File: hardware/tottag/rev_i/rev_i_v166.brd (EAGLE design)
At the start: 68.1 x 36.9 mm, 185 parts, among them J1 USB4110-GF-A, J2 TC2030-JLINK-NL-2SIDE, J3 TC2030-JLINK-NL-2SIDE, J4 MOLEX-PICO-SPOX-3SIDE, Q1 CSD75207W15, Q2 MOSFET-NCHANNELXFDN-3, U1 APOLLO4_BLUE_SOC_BGA, U2 DW3210, U3 BQ24040, U4 BQ51013B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

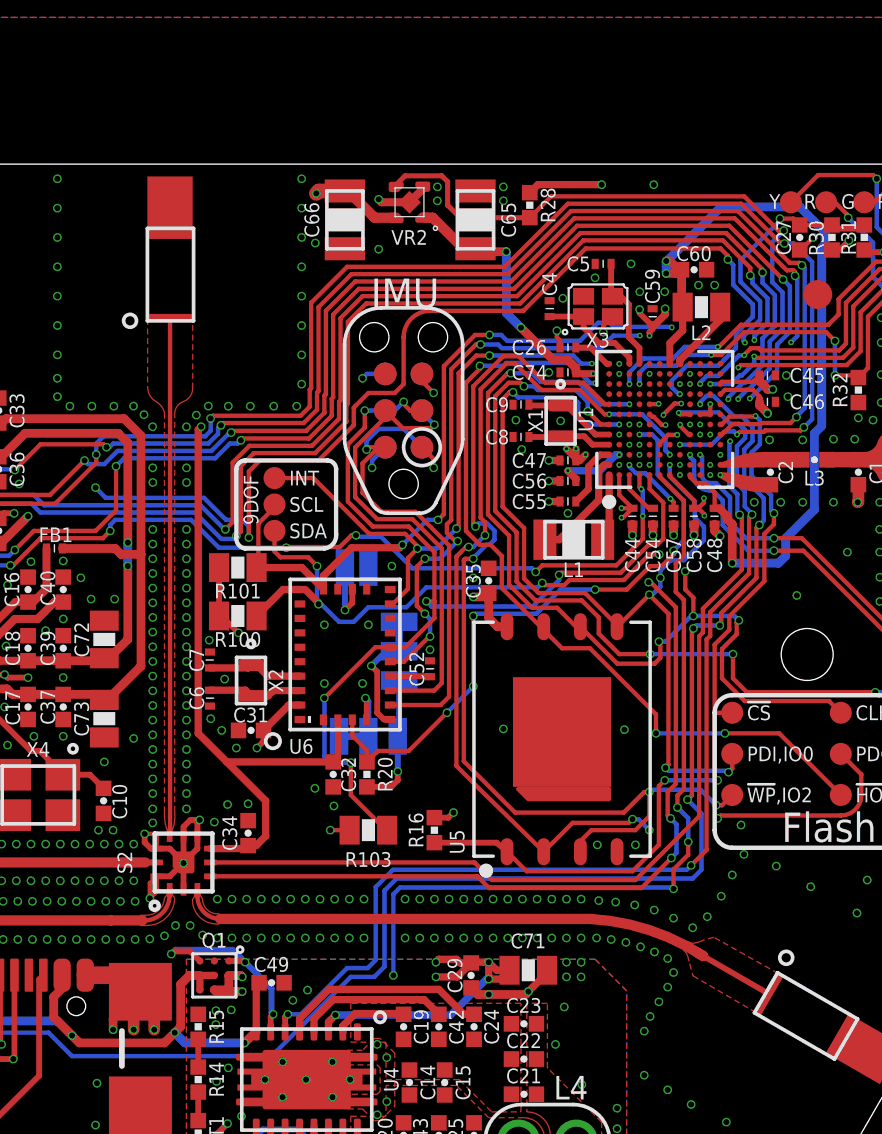
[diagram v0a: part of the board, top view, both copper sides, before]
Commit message: fix VR2 footprint; add BOM
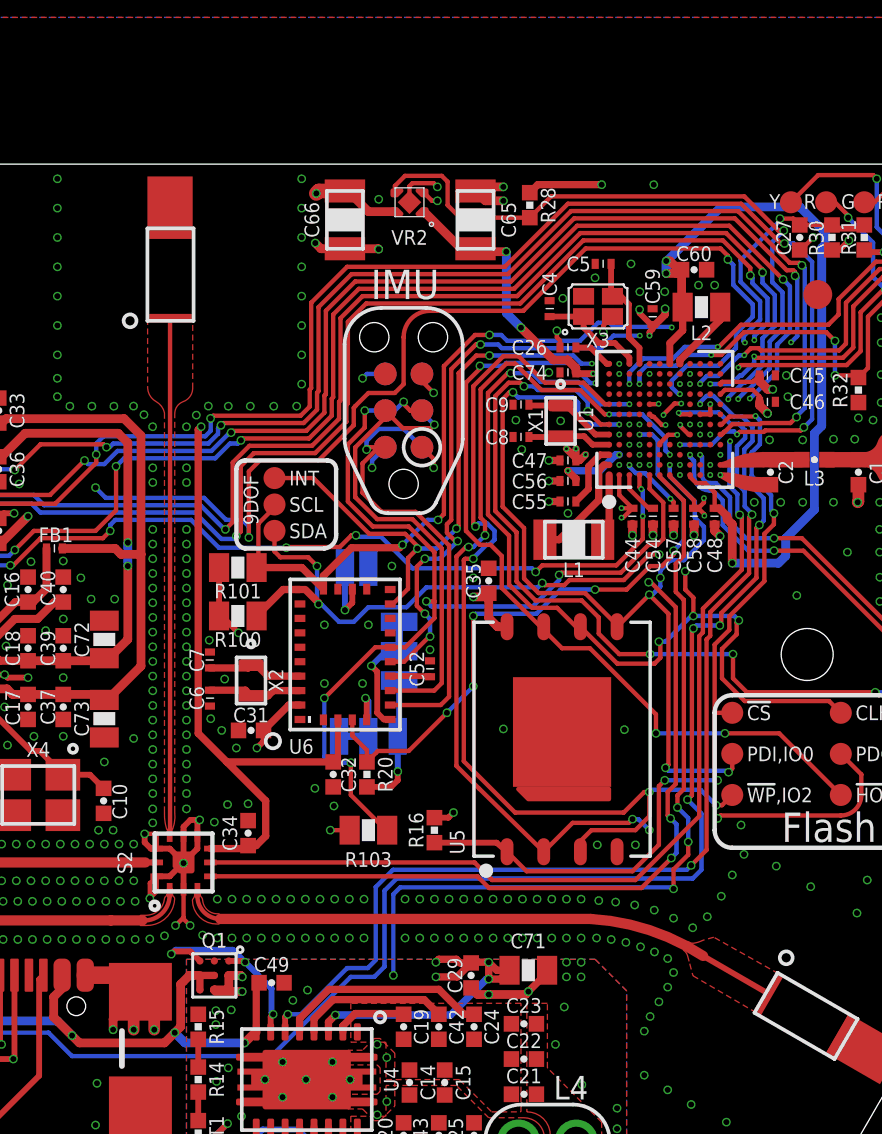
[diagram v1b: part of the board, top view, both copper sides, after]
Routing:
- net GND: track 103.4 -> 109.9 mm
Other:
- board text removed: "STM"
- board text removed: "nRF"
